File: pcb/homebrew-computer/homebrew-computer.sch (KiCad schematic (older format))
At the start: 0 parts

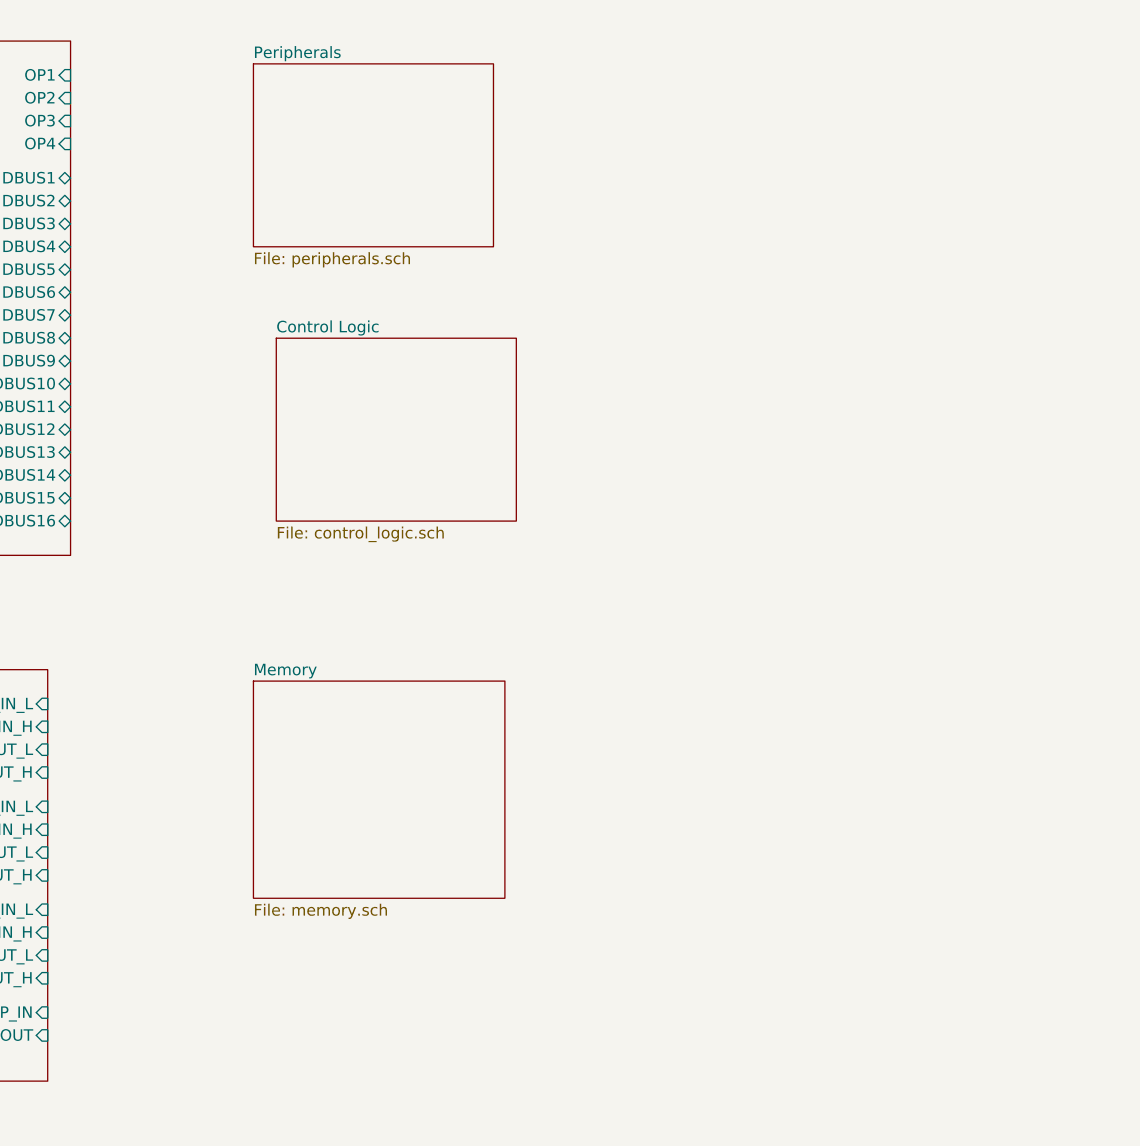
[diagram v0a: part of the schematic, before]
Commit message: Add part of the control logic
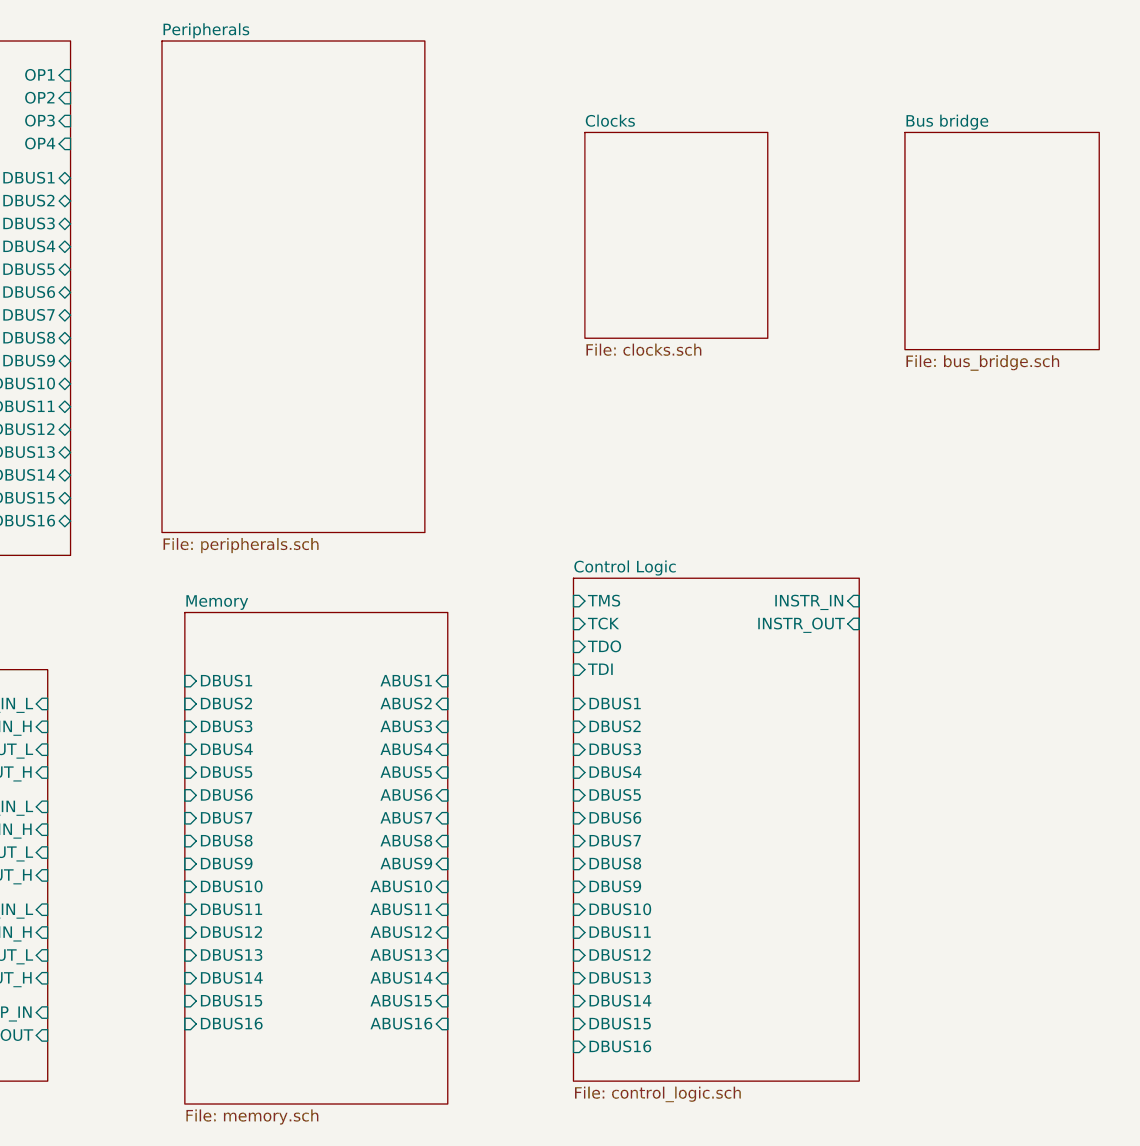
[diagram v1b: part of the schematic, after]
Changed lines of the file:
@@
 $Descr A4 11693 8268
 encoding utf-8
-Sheet 1 5
+Sheet 1 7
 Title "Homebrew Computer"
 Date "2020-10-17"
@@
 $EndDescr
 $Sheet
-S 4250 1100 1050 800
+S 3850 1000 1150 2150
 U 5F8B5DB4
 F0 "Peripherals" 50
@@
 $EndSheet
 $Sheet
-S 4350 2300 1050 800
+S 5650 3350 1250 2200
 U 5F8B5E3D
 F0 "Control Logic" 50
 F1 "control_logic.sch" 50
+F2 "TMS" I L 5650 3450 50
+F3 "TCK" I L 5650 3550 50
+F4 "TDO" I L 5650 3650 50
+F5 "TDI" I L 5650 3750 50
+F6 "DBUS1" I L 5650 3900 50
+F7 "DBUS2" I L 5650 4000 50
+F8 "DBUS3" I L 5650 4100 50
+F9 "DBUS4" I L 5650 4200 50
+F10 "DBUS5" I L 5650 4300 50
+F11 "DBUS6" I L 5650 4400 50
+F12 "DBUS7" I L 5650 4500 50
+F13 "DBUS8" I L 5650 4600 50
+F14 "DBUS9" I L 5650 4700 50
+F15 "DBUS10" I L 5650 4800 50
+F16 "DBUS11" I L 5650 4900 50
+F17 "DBUS12" I L 5650 5000 50
+F18 "DBUS13" I L 5650 5100 50
+F19 "DBUS14" I L 5650 5200 50
+F20 "DBUS15" I L 5650 5300 50
+F21 "DBUS16" I L 5650 5400 50
+F22 "INSTR_IN" I R 6900 3450 50
+F23 "INSTR_OUT" I R 6900 3550 50
 $EndSheet
 $Sheet
@@
 $EndSheet
 $Sheet
-S 4250 3800 1100 950
+S 3950 3500 1150 2150
 U 5F95DC76
 F0 "Memory" 50
 F1 "memory.sch" 50
+F2 "DBUS1" I L 3950 3800 50
+F3 "DBUS2" I L 3950 3900 50
+F4 "DBUS3" I L 3950 4000 50
+F5 "DBUS4" I L 3950 4100 50
+F6 "DBUS5" I L 3950 4200 50
+F7 "DBUS6" I L 3950 4300 50
+F8 "DBUS7" I L 3950 4400 50
+F9 "DBUS8" I L 3950 4500 50
+F10 "DBUS9" I L 3950 4600 50
+F11 "DBUS10" I L 3950 4700 50
+F12 "DBUS11" I L 3950 4800 50
+F13 "DBUS12" I L 3950 4900 50
+F14 "DBUS13" I L 3950 5000 50
+F15 "DBUS14" I L 3950 5100 50
+F16 "DBUS15" I L 3950 5200 50
+F17 "DBUS16" I L 3950 5300 50
+F18 "ABUS1" I R 5100 3800 50
+F19 "ABUS2" I R 5100 3900 50
+F20 "ABUS3" I R 5100 4000 50
+F21 "ABUS4" I R 5100 4100 50
+F22 "ABUS5" I R 5100 4200 50
+F23 "ABUS6" I R 5100 4300 50
+F24 "ABUS7" I R 5100 4400 50
+F25 "ABUS8" I R 5100 4500 50
+F26 "ABUS9" I R 5100 4600 50
+F27 "ABUS10" I R 5100 4700 50
+F28 "ABUS11" I R 5100 4800 50
+F29 "ABUS12" I R 5100 4900 50
+F30 "ABUS13" I R 5100 5000 50
+F31 "ABUS14" I R 5100 5100 50
+F32 "ABUS15" I R 5100 5200 50
+F33 "ABUS16" I R 5100 5300 50
+$EndSheet
+$Sheet
+S 5700 1400 800  900
+U 5F97DC64
+F0 "Clocks" 50
+F1 "clocks.sch" 50
+$EndSheet
+$Sheet
+S 7100 1400 850  950
+U 5F97DCB2
+F0 "Bus bridge" 50
+F1 "bus_bridge.sch" 50
 $EndSheet
 $EndSCHEMATC

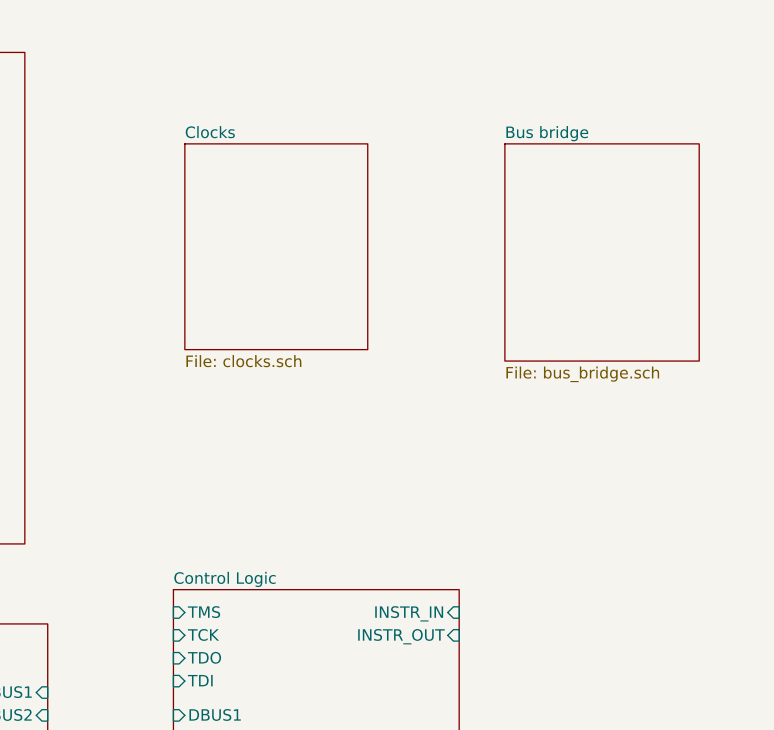
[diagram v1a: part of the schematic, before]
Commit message: Add clock generation
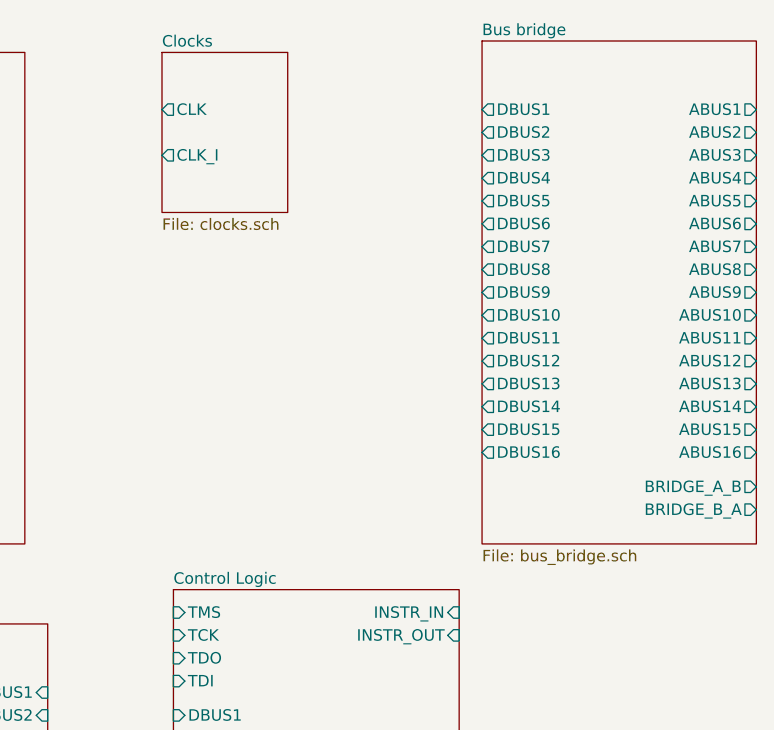
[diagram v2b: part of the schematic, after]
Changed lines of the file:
@@
 $Descr A4 11693 8268
 encoding utf-8
-Sheet 1 7
+Sheet 1 8
 Title "Homebrew Computer"
 Date "2020-10-17"
@@
 $EndSheet
 $Sheet
-S 5700 1400 800  900
+S 5600 1000 550  700
 U 5F97DC64
 F0 "Clocks" 50
 F1 "clocks.sch" 50
-$EndSheet
-$Sheet
-S 7100 1400 850  950
+F2 "CLK" O L 5600 1250 50
+F3 "CLK_I" O L 5600 1450 50
+$EndSheet
+$Sheet
+S 7000 950  1200 2200
 U 5F97DCB2
 F0 "Bus bridge" 50
 F1 "bus_bridge.sch" 50
+F2 "DBUS1" O L 7000 1250 50
+F3 "DBUS2" O L 7000 1350 50
+F4 "DBUS3" O L 7000 1450 50
+F5 "DBUS4" O L 7000 1550 50
+F6 "DBUS5" O L 7000 1650 50
+F7 "DBUS6" O L 7000 1750 50
+F8 "DBUS7" O L 7000 1850 50
+F9 "DBUS8" O L 7000 1950 50
+F10 "DBUS9" O L 7000 2050 50
+F11 "DBUS10" O L 7000 2150 50
+F12 "DBUS11" O L 7000 2250 50
+F13 "DBUS12" O L 7000 2350 50
+F14 "DBUS13" O L 7000 2450 50
+F15 "DBUS14" O L 7000 2550 50
+F16 "DBUS15" O L 7000 2650 50
+F17 "DBUS16" O L 7000 2750 50
+F18 "ABUS1" O R 8200 1250 50
+F19 "ABUS2" O R 8200 1350 50
+F20 "ABUS3" O R 8200 1450 50
+F21 "ABUS4" O R 8200 1550 50
+F22 "ABUS5" O R 8200 1650 50
+F23 "ABUS6" O R 8200 1750 50
+F24 "ABUS7" O R 8200 1850 50
+F25 "ABUS8" O R 8200 1950 50
+F26 "ABUS9" O R 8200 2050 50
+F27 "ABUS10" O R 8200 2150 50
+F28 "ABUS11" O R 8200 2250 50
+F29 "ABUS12" O R 8200 2350 50
+F30 "ABUS13" O R 8200 2450 50
+F31 "ABUS14" O R 8200 2550 50
+F32 "ABUS15" O R 8200 2650 50
+F33 "ABUS16" O R 8200 2750 50
+F34 "BRIDGE_A_B" O R 8200 2900 50
+F35 "BRIDGE_B_A" O R 8200 3000 50
 $EndSheet
 $EndSCHEMATC

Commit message: Add resistor nets for bus termination
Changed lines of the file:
@@
 $EndSheet
 $Sheet
-S 2300 3750 1050 1800
+S 2250 3650 1050 1800
 U 5F8C07F0
 F0 "Registers" 50
 F1 "registers.sch" 50
-F2 "DBUS1" I L 2300 3900 50
-F3 "DBUS2" I L 2300 4000 50
-F4 "DBUS3" I L 2300 4100 50
-F5 "DBUS4" I L 2300 4200 50
-F6 "DBUS5" I L 2300 4300 50
-F7 "DBUS6" I L 2300 4400 50
-F8 "DBUS7" I L 2300 4500 50
-F9 "DBUS8" I L 2300 4600 50
-F10 "DBUS9" I L 2300 4700 50
-F11 "DBUS10" I L 2300 4800 50
-F12 "DBUS11" I L 2300 4900 50
-F13 "DBUS12" I L 2300 5000 50
-F14 "DBUS13" I L 2300 5100 50
-F15 "DBUS14" I L 2300 5200 50
-F16 "DBUS15" I L 2300 5300 50
-F17 "DBUS16" I L 2300 5400 50
-F18 "REG1_IN_L" I R 3350 3900 50
-F19 "REG1_IN_H" I R 3350 4000 50
-F20 "REG1_OUT_L" I R 3350 4100 50
-F21 "REG1_OUT_H" I R 3350 4200 50
-F22 "REG2_IN_L" I R 3350 4350 50
-F23 "REG2_IN_H" I R 3350 4450 50
-F24 "REG2_OUT_L" I R 3350 4550 50
-F25 "REG2_OUT_H" I R 3350 4650 50
-F26 "REG3_IN_L" I R 3350 4800 50
-F27 "REG3_IN_H" I R 3350 4900 50
-F28 "REG3_OUT_L" I R 3350 5000 50
-F29 "REG3_OUT_H" I R 3350 5100 50
-F30 "SP_IN" I R 3350 5250 50
-F31 "SP_OUT" I R 3350 5350 50
+F2 "DBUS1" I L 2250 3800 50
+F3 "DBUS2" I L 2250 3900 50
+F4 "DBUS3" I L 2250 4000 50
+F5 "DBUS4" I L 2250 4100 50
+F6 "DBUS5" I L 2250 4200 50
+F7 "DBUS6" I L 2250 4300 50
+F8 "DBUS7" I L 2250 4400 50
+F9 "DBUS8" I L 2250 4500 50
+F10 "DBUS9" I L 2250 4600 50
+F11 "DBUS10" I L 2250 4700 50
+F12 "DBUS11" I L 2250 4800 50
+F13 "DBUS12" I L 2250 4900 50
+F14 "DBUS13" I L 2250 5000 50
+F15 "DBUS14" I L 2250 5100 50
+F16 "DBUS15" I L 2250 5200 50
+F17 "DBUS16" I L 2250 5300 50
+F18 "REG1_IN_L" I R 3300 3800 50
+F19 "REG1_IN_H" I R 3300 3900 50
+F20 "REG1_OUT_L" I R 3300 4000 50
+F21 "REG1_OUT_H" I R 3300 4100 50
+F22 "REG2_IN_L" I R 3300 4250 50
+F23 "REG2_IN_H" I R 3300 4350 50
+F24 "REG2_OUT_L" I R 3300 4450 50
+F25 "REG2_OUT_H" I R 3300 4550 50
+F26 "REG3_IN_L" I R 3300 4700 50
+F27 "REG3_IN_H" I R 3300 4800 50
+F28 "REG3_OUT_L" I R 3300 4900 50
+F29 "REG3_OUT_H" I R 3300 5000 50
+F30 "SP_IN" I R 3300 5150 50
+F31 "SP_OUT" I R 3300 5250 50
 $EndSheet
 $Sheet
@@
 S 7000 950  1200 2200
 U 5F97DCB2
-F0 "Bus bridge" 50
-F1 "bus_bridge.sch" 50
+F0 "Bus logic" 50
+F1 "bus_logic.sch" 50
 F2 "DBUS1" O L 7000 1250 50
 F3 "DBUS2" O L 7000 1350 50
@@
 F32 "ABUS15" O R 8200 2650 50
 F33 "ABUS16" O R 8200 2750 50
-F34 "BRIDGE_A_B" O R 8200 2900 50
-F35 "BRIDGE_B_A" O R 8200 3000 50
+F34 "A_TO_B" O R 8200 2900 50
+F35 "BRIDGE" O R 8200 3000 50
 $EndSheet
 $EndSCHEMATC
